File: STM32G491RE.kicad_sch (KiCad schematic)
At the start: 20 parts, among them J2 Conn_01x24, J3 Conn_01x25, J9 Conn_01x06, M15 Motor_DC, SW2 SW_Push, U2 STM32G491RETx, Y1 24MHz, Y2 32.768KHz

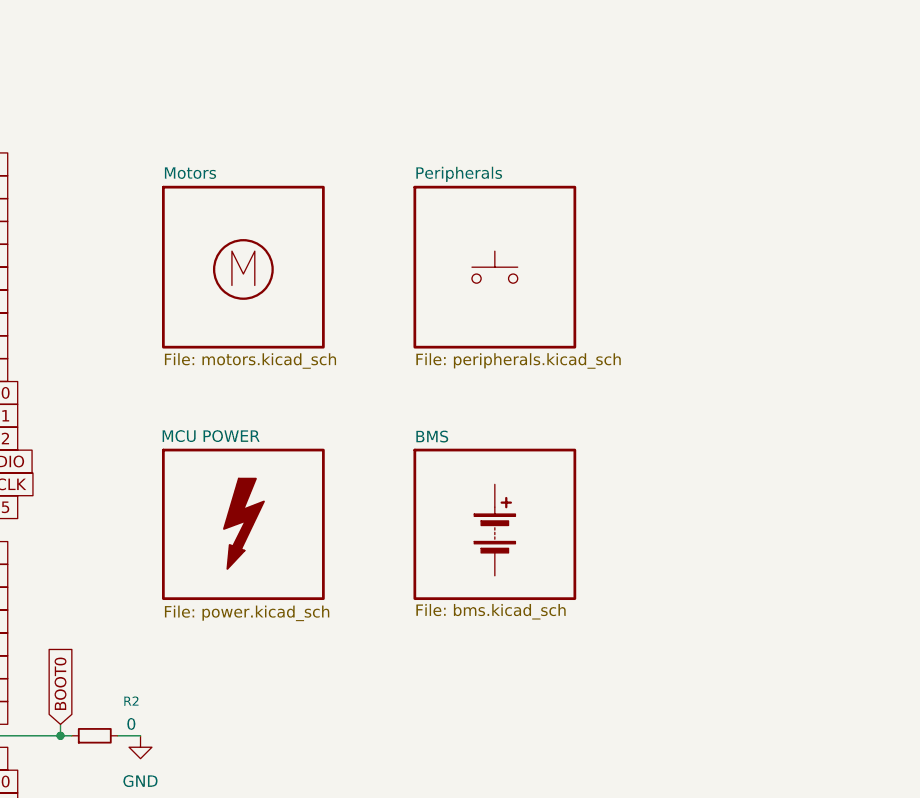
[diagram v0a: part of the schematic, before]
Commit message: finalized parts before sensors
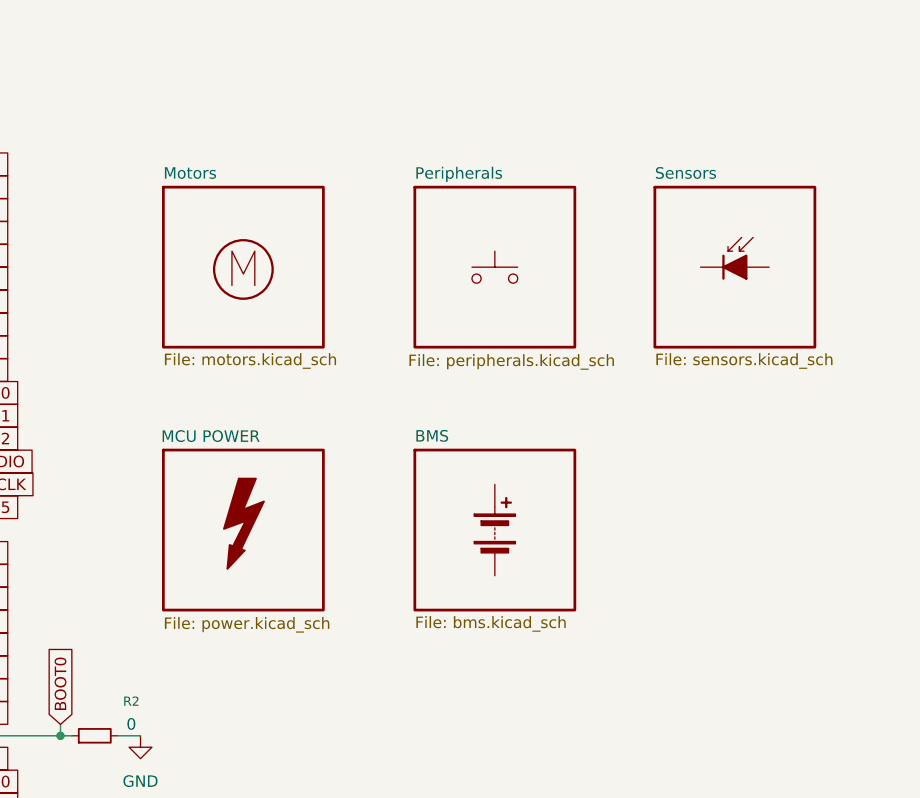
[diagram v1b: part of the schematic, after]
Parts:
- added D99: (no value), symbol Device:D_Photo_Filled
- C1, C2, C3, C4: footprint Capacitor_SMD:C_0402_1005Metric_Pad0.74x0.62mm_HandSolder -> Capacitor_SMD:C_0805_2012Metric_Pad1.18x1.45mm_HandSolder
- C21: footprint (none) -> Capacitor_SMD:C_0805_2012Metric_Pad1.18x1.45mm_HandSolder
- C5: footprint Resistor_SMD:R_0402_1005Metric_Pad0.72x0.64mm_HandSolder -> Capacitor_SMD:C_0805_2012Metric_Pad1.18x1.45mm_HandSolder
- D2_ON1: footprint (none) -> LED_SMD:LED_0805_2012Metric_Pad1.15x1.40mm_HandSolder
- R1, R2: footprint Resistor_SMD:R_0402_1005Metric_Pad0.72x0.64mm_HandSolder -> Resistor_SMD:R_0805_2012Metric_Pad1.20x1.40mm_HandSolder
- R3: footprint (none) -> Resistor_SMD:R_0805_2012Metric_Pad1.20x1.40mm_HandSolder
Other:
- added sheet Sensors (sensors.kicad_sch)
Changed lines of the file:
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@@
 			)
 		)
-		(property "Footprint" "Capacitor_SMD:C_0402_1005Metric_Pad0.74x0.62mm_HandSolder"
+		(property "Footprint" "Capacitor_SMD:C_0805_2012Metric_Pad1.18x1.45mm_HandSolder"
 			(at 27.94 46.99 0)
 			(hide yes)
@@
 			)
 		)
-		(property "Footprint" "Capacitor_SMD:C_0402_1005Metric_Pad0.74x0.62mm_HandSolder"
+		(property "Footprint" "Capacitor_SMD:C_0805_2012Metric_Pad1.18x1.45mm_HandSolder"
 			(at 27.94 66.04 0)
 			(hide yes)
@@
 		(unit 1)
 		(body_style 1)
-		(exclude_from_sim yes)
+		(exclude_from_sim no)
 		(in_bom no)
 		(on_board no)
@@
 			)
 		)
-		(property "Footprint" ""
+		(property "Footprint" "Capacitor_SMD:C_0805_2012Metric_Pad1.18x1.45mm_HandSolder"
 			(at 43.18 25.4 0)
 			(hide yes)
@@
 			)
 		)
-		(property "Footprint" "Resistor_SMD:R_0402_1005Metric_Pad0.72x0.64mm_HandSolder"
+		(property "Footprint" "Resistor_SMD:R_0805_2012Metric_Pad1.20x1.40mm_HandSolder"
 			(at 43.18 134.62 0)
 			(hide yes)
@@
 			)
 		)
-		(property "Footprint" "Capacitor_SMD:C_0402_1005Metric_Pad0.74x0.62mm_HandSolder"
+		(property "Footprint" "Capacitor_SMD:C_0805_2012Metric_Pad1.18x1.45mm_HandSolder"
 			(at 27.94 54.61 0)
 			(hide yes)
@@
 			)
 		)
-		(property "Footprint" "Capacitor_SMD:C_0402_1005Metric_Pad0.74x0.62mm_HandSolder"
+		(property "Footprint" "Capacitor_SMD:C_0805_2012Metric_Pad1.18x1.45mm_HandSolder"
 			(at 27.94 73.66 0)
 			(hide yes)
@@
 			)
 		)
-		(property "Footprint" "Resistor_SMD:R_0402_1005Metric_Pad0.72x0.64mm_HandSolder"
+		(property "Footprint" "Capacitor_SMD:C_0805_2012Metric_Pad1.18x1.45mm_HandSolder"
 			(at 43.18 142.24 0)
 			(hide yes)
@@
 	)
 	(symbol
+		(lib_id "Device:D_Photo_Filled")
+		(at 209.55 39.37 0)
+		(unit 1)
+		(body_style 1)
+		(exclude_from_sim no)
+		(in_bom yes)
+		(on_board yes)
+		(in_pos_files yes)
+		(dnp no)
+		(fields_autoplaced yes)
+		(property "Reference" "D99"
+			(at 208.5975 31.75 0)
+			(hide yes)
+			(show_name no)
+			(do_not_autoplace no)
+			(effects
+				(font
+					(size 1.27 1.27)
+				)
+			)
+		)
+		(property "Value" ""
+			(at 208.5975 34.29 0)
+			(hide yes)
+			(show_name no)
+			(do_not_autoplace no)
+			(effects
+				(font
+					(size 1.27 1.27)
+				)
+			)
+		)
+		(property "Footprint" ""
+			(at 208.28 39.37 0)
+			(hide yes)
+			(show_name no)
+			(do_not_autoplace no)
+			(effects
+				(font
+					(size 1.27 1.27)
+				)
+			)
+		)
+		(property "Datasheet" ""
+			(at 208.28 39.37 0)
+			(hide yes)
+			(show_name no)
+			(do_not_autoplace no)
+			(effects
+				(font
+					(size 1.27 1.27)
+				)
+			)
+		)
+		(property "Description" "Photodiode, filled shape"
+			(at 209.55 39.37 0)
+			(hide yes)
+			(show_name no)
+			(do_not_autoplace no)
+			(effects
+				(font
+					(size 1.27 1.27)
+				)
+			)
+		)
+		(pin "1"
+		)
+		(pin "2"
+		)
+		(instances
+			(project "STM32G491RE"
+				(path "/213f8898-394f-49c4-9e4a-d0dfd12ebcad"
+					(reference "D99")
+					(unit 1)
+				)
+			)
+		)
+	)
+	(symbol
 		(lib_id "power:GND")
 		(at 60.96 69.85 0)
@@
 			)
 		)
-		(property "Footprint" ""
+		(property "Footprint" "Resistor_SMD:R_0805_2012Metric_Pad1.20x1.40mm_HandSolder"
 			(at 60.96 59.69 0)
 			(hide yes)
@@
 			)
 		)
-		(property "Footprint" ""
+		(property "Footprint" "LED_SMD:LED_0805_2012Metric_Pad1.15x1.40mm_HandSolder"
 			(at 60.96 66.04 0)
 			(hide yes)
@@
 			)
 		)
-		(property "Footprint" "Resistor_SMD:R_0402_1005Metric_Pad0.72x0.64mm_HandSolder"
+		(property "Footprint" "Resistor_SMD:R_0805_2012Metric_Pad1.20x1.40mm_HandSolder"
 			(at 137.16 91.44 0)
 			(hide yes)
@@
 		(on_board yes)
 		(dnp no)
-		(fields_autoplaced yes)
 		(stroke
 			(width 0.3048)
@@
 		)
 		(property "Sheetfile" "peripherals.kicad_sch"
-			(at 172.72 48.9208 0)
+			(at 171.958 49.022 0)
 			(show_name no)
 			(do_not_autoplace no)
@@
 	(sheet
 		(at 144.78 59.69)
-		(size 17.78 16.51)
+		(size 17.78 17.78)
 		(exclude_from_sim no)
 		(in_bom yes)
@@
 		)
 		(property "Sheetfile" "power.kicad_sch"
-			(at 144.78 76.962 0)
+			(at 144.78 78.232 0)
 			(show_name no)
 			(do_not_autoplace no)
@@
 	)
 	(sheet
+		(at 199.39 30.48)
+		(size 17.78 17.78)
+		(exclude_from_sim no)
+		(in_bom yes)
+		(on_board yes)
+		(dnp no)
+		(fields_autoplaced yes)
+		(stroke
+			(width 0.3048)
+			(type solid)
+		)
+		(fill
+			(color 255 255 194 1)
+		)
+		(property "Sheetname" "Sensors"
+			(at 199.39 29.6922 0)
+			(show_name no)
+			(do_not_autoplace no)
+			(effects
+				(font
+					(size 1.27 1.27)
+				)
+				(justify left bottom)
+			)
+		)
+		(property "Sheetfile" "sensors.kicad_sch"
+			(at 199.39 48.9208 0)
+			(show_name no)
+			(do_not_autoplace no)
+			(effects
+				(font
+					(size 1.27 1.27)
+				)
+				(justify left top)
+			)
+		)
+		(instances
+			(project "STM32G491RE"
+				(path "/213f8898-394f-49c4-9e4a-d0dfd12ebcad"
+					(page "6")
+				)
+			)
+		)
+	)
+	(sheet
 		(at 172.72 59.69)
-		(size 17.78 16.51)
+		(size 17.78 17.78)
 		(exclude_from_sim no)
 		(in_bom yes)
@@
 		)
 		(property "Sheetname" "BMS"
-			(at 172.72 58.9784 0)
+			(at 172.72 58.9022 0)
 			(show_name no)
 			(do_not_autoplace no)
@@
 		)
 		(property "Sheetfile" "bms.kicad_sch"
-			(at 172.72 76.7846 0)
+			(at 172.72 78.1308 0)
 			(show_name no)
 			(do_not_autoplace no)

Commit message: slightly change schematic, making sure everything is ok, preparing for finalization
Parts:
- removed R1: 10K, Resistor_SMD:R_0805_2012Metric_Pad1.20x1.40mm_HandSolder, symbol Device:R_Small
- added Ce1: 100nF, Capacitor_SMD:C_0805_2012Metric_Pad1.18x1.45mm_HandSolder, symbol Device:C_Small
- added R56: 2k, Resistor_SMD:R_0805_2012Metric_Pad1.20x1.40mm_HandSolder, symbol Device:R_Small
- added U11: TSOP38238, kicad_custom:TSOP382, symbol TSOP382:TSOP38238
- J9: value Conn_01x06 -> Conn_01x10; footprint (none) -> Connector_PinHeader_2.54mm:PinHeader_1x06_P2.54mm_Vertical; symbol Connector_Generic:Conn_01x06 -> Connector_Generic:Conn_01x10
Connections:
- net +3V3: now also J9.8 (Pin_8), R56.2; no longer J9.6 (Pin_6)
- net BOOT0: now also J9.7 (Pin_7); no longer J9.5 (Pin_5)
- net GND: now also Ce1.2, U11.2 (GND)
- net R: now also J9.4 (Pin_4); no longer J9.2 (Pin_2)
- net SWCLK: now also J9.5 (Pin_5); no longer J9.3 (Pin_3)
- net SWDIO: now also J9.6 (Pin_6); no longer J9.4 (Pin_4)
- net USART1_RX: now also J9.2 (Pin_2)
- net USART1_TX: now also J9.3 (Pin_3)
- net PA8 renamed SDA
- net PA9 renamed SCL
- new net: Ce1.1, R56.1, U11.3 (VS)
- new net +5V: J9.9 (Pin_9)
- new net ON/OFF IR signal: U11.1 (OUT)
- no-connect marks 0 -> 1
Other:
- note added: "5V+"
- note added: "I2C2"
- note added: "IR RECEIVER"
- note added: "TODO: assign all these connections to GPIO pins"
- note removed: "5V-40V UNREGULATED"
- moved on the sheet: BTN8, C1, C2, C21, C3, C4, C5, D2_ON1, J2, J3, R2, R3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
